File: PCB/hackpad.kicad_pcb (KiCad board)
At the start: 2 copper layers, 40.5 x 84 mm, 9 parts, among them SW1 SW_Push, SW2 SW_Push, SW3 SW_Push, SW4 SW_Push, SW5 SW_Push, SW6 SW_Push, U1 XIAO-RP2040-DIP

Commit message: Adding Feedback
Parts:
- removed SW6: SW_Push, Button_Switch_Keyboard:SW_Cherry_MX_1.00u_PCB
- added SW7: RotaryEncoder_Switch, Rotary_Encoder:RotaryEncoder_Alps_EC11E-Switch_Vertical_H20mm, F.Cu at (113.2, 134.0)
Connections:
- U1 pad 3: unconnected-(U1-GPIO28/ADC2/A2-Pad3) -> Net-(U1-GPIO28/ADC2/A2)
- U1 pad 4: unconnected-(U1-GPIO29/ADC3/A3-Pad4) -> Net-(U1-GPIO29/ADC3/A3)
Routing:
- net Net-(U1-GPIO29/ADC3/A3): track 0.00 -> 120.8 mm
- net GND: track 235.5 -> 210.4 mm
- net Net-(U1-GPIO26/ADC0/A0): track 96.8 -> 98.9 mm

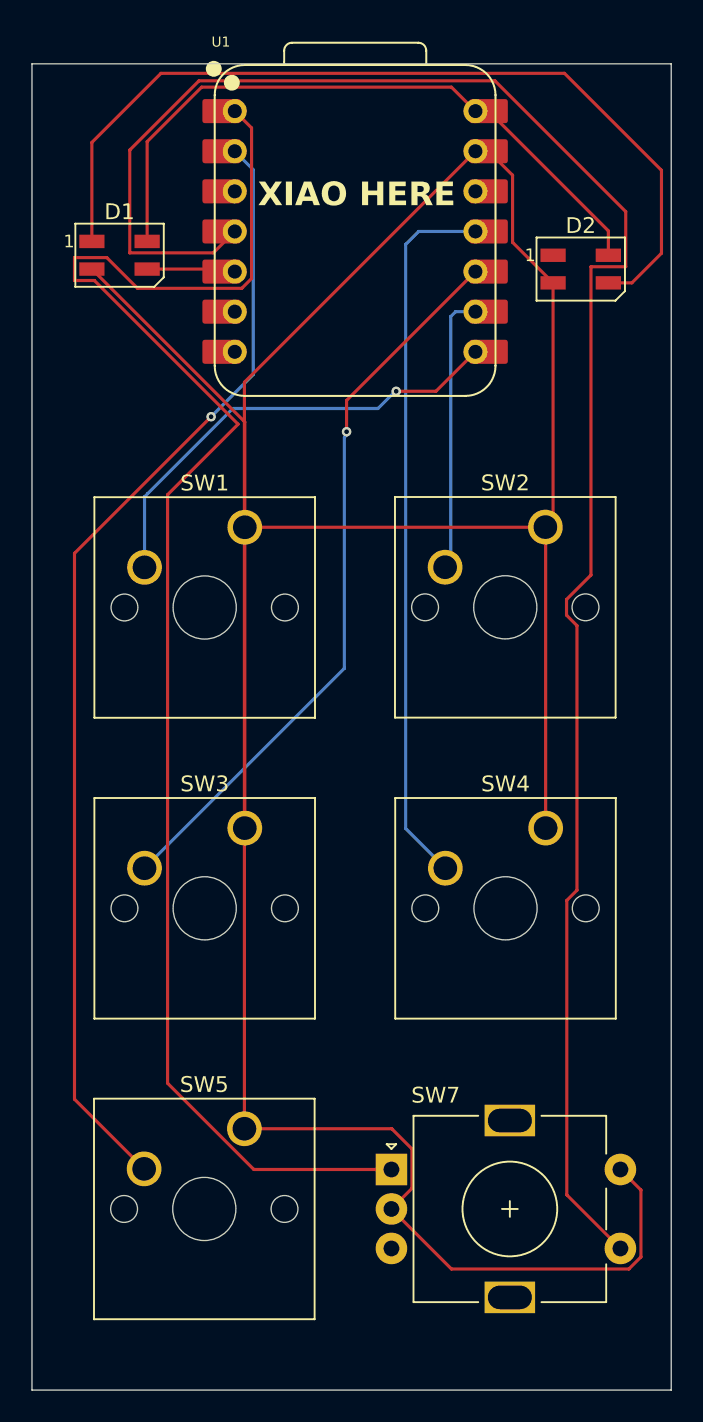
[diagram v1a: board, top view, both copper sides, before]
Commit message: Changing SK6812 to SK6812 MINI LEDS
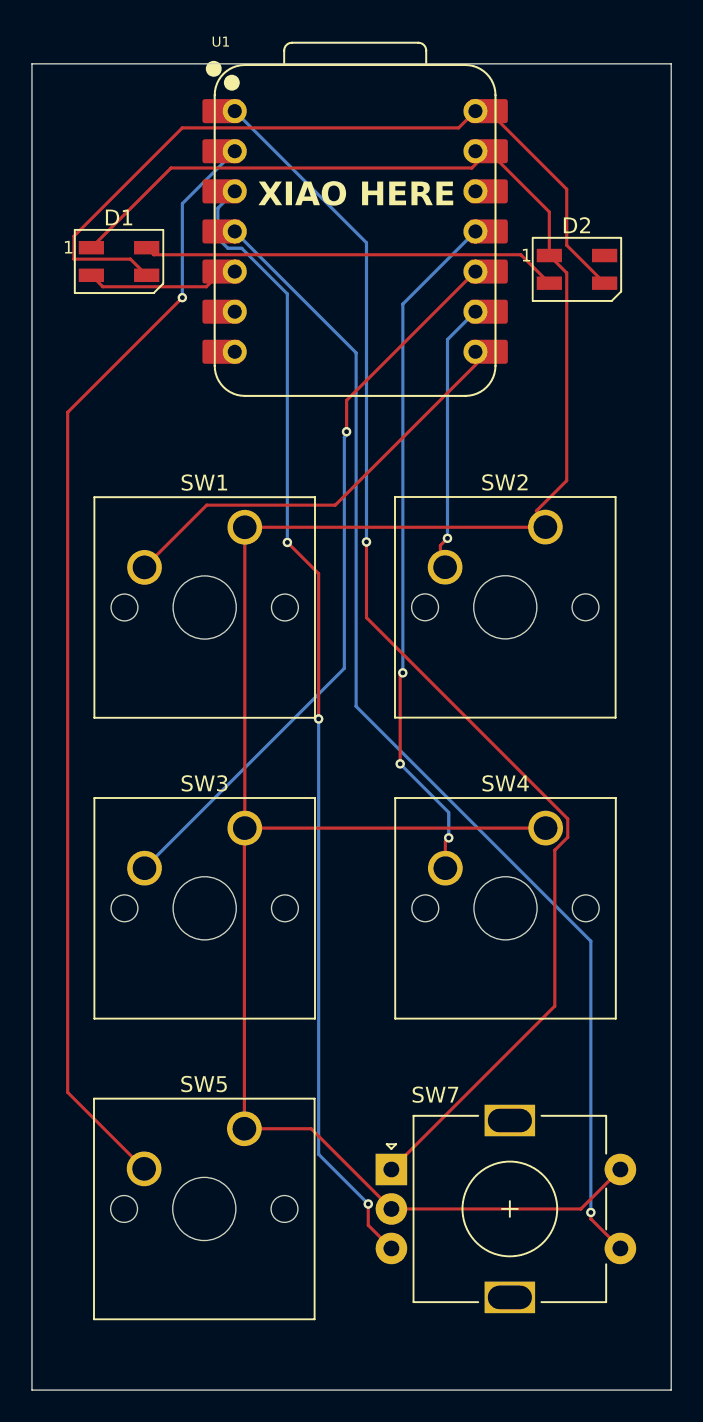
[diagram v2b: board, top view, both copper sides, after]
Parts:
- D1, D2: value SK6812MINI -> SK6812
- moved D1 0.40 mm to (96.0, 76.5)
- moved D2 0.24 mm to (125.0, 77.0)
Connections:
- D1 pad 1: Net-(D1-DOUT) -> GND
- D1 pad 2: GND -> Net-(D1-DIN)
- D1 pad 3: Net-(D1-DIN) -> +5V
- D1 pad 4: +5V -> Net-(D1-DOUT)
- D2 pad 1: unconnected-(D2-DOUT-Pad1) -> GND
- D2 pad 2: GND -> Net-(D1-DOUT)
- D2 pad 3: Net-(D1-DOUT) -> +5V
- D2 pad 4: +5V -> unconnected-(D2-DOUT-Pad4)
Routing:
- net Net-(U1-GPIO28/ADC2/A2): track 0.00 -> 72.4 mm, vias 0 -> 3
- net GND: track 210.4 -> 157.7 mm
- net Net-(U1-GPIO29/ADC3/A3): track 120.8 -> 74.5 mm, vias 0 -> 1
- net Net-(D1-DOUT): track 56.1 -> 26.4 mm
- net Net-(U1-GPIO26/ADC0/A0): track 98.9 -> 80.4 mm, vias 0 -> 1
- net +5V: track 41.4 -> 49.1 mm
- net Net-(D1-DIN): track 5.61 -> 8.94 mm
- net Net-(U1-GPIO1/RX): track 29.2 -> 27.4 mm, vias 1 -> 0
- net Net-(U1-GPIO3/MOSI): track 45.3 -> 43.7 mm, vias 0 -> 3
- net Net-(U1-GPIO27/ADC1/A1): track 71.4 -> 70.8 mm
- net Net-(U1-GPIO2/SCK): track 17.8 -> 17.2 mm, vias 0 -> 1
